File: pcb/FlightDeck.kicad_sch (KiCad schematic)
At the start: 4 parts, among them J1 Conn_02x08_Odd_Even_MountingP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, J2 Conn_01x19_MountingPin, J3 Conn_01x19_MountingPin, U1 ESP32-DEVKITC-32E

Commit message: New PCB and hardware details
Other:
- title: (none) -> FlightDeck Adapter PCB
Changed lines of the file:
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@@
 	(generator_version "9.0")
 	(paper "A4")
+	(title_block
+		(title "FlightDeck Adapter PCB")
+		(date "2026-01-12")
+	)
 	(junction
 		(at 151.13 118.11)

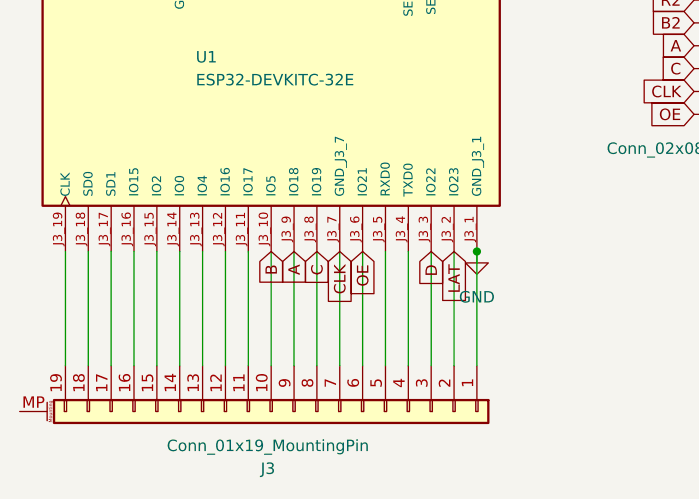
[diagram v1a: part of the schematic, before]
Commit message: Updated firmware to not use circuitpython
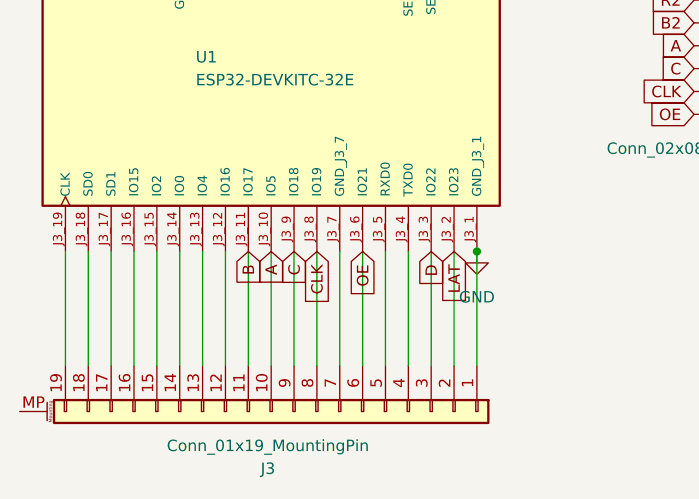
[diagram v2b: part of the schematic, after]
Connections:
- net A: now also J3.10 (Pin_10), U1.J3_10 (IO5); no longer J3.9 (Pin_9), U1.J3_9 (IO18)
- net B: now also J3.11 (Pin_11), U1.J3_11 (IO17); no longer J3.10 (Pin_10), U1.J3_10 (IO5)
- net C: now also J3.9 (Pin_9), U1.J3_9 (IO18); no longer J3.8 (Pin_8), U1.J3_8 (IO19)
- net CLK: now also J3.8 (Pin_8), U1.J3_8 (IO19); no longer J3.7 (Pin_7), U1.J3_7 (GND_J3_7)
- new net: J3.7 (Pin_7), U1.J3_7 (GND_J3_7)
